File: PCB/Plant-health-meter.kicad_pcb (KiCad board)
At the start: 4 copper layers, 121.2 x 25 mm, 74 parts, among them J1 Conn_01x02, J2 Conn_01x02, J3 Conn_01x04, J4 UJ2-MIBH2-4-SMT-TR, J5 Conn_01x02, Q1 AO3401A, SW1 Boot, SW2 Reset, U1 LTC4412xS6, U2 TPS62172DSG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

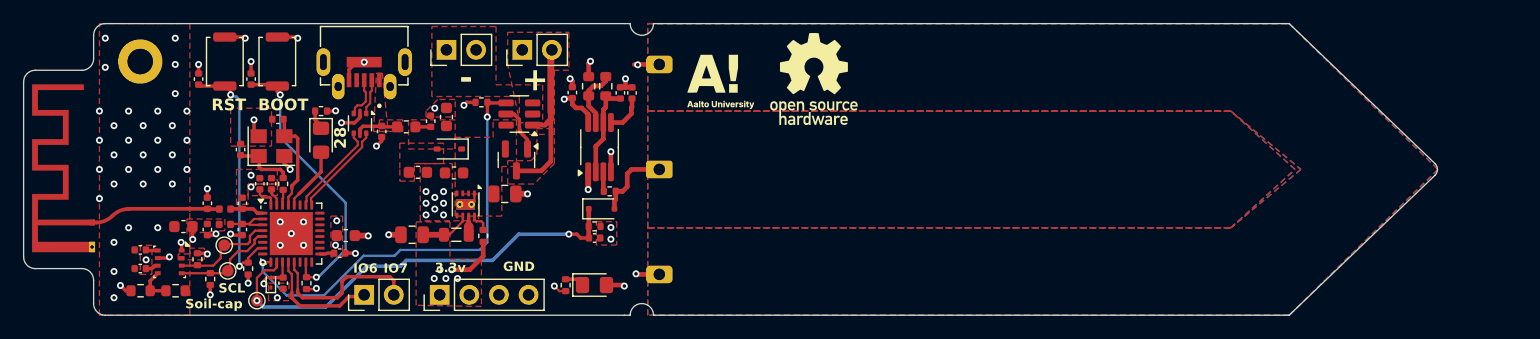
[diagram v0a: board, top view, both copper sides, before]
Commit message: Added battery charging circuit and created WiFi api in firmware + created simple server for esp to send data to
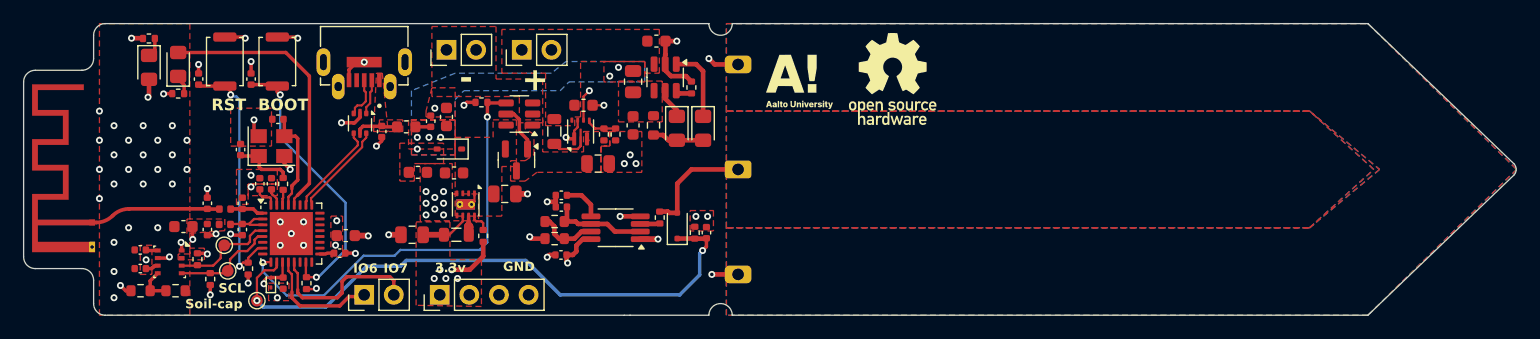
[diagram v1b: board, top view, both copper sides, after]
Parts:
- removed H1: MountingHole, MountingHole:MountingHole_2.2mm_M2_DIN965_Pad
- added C1: 10u, Capacitor_SMD:C_0603_1608Metric, F.Cu at (142.0, 107.0)
- added C27: 10u, Capacitor_SMD:C_0603_1608Metric, F.Cu at (148.2, 101.5)
- added C28: 22u, Capacitor_SMD:C_0805_2012Metric, F.Cu at (143.2, 112.0)
- added C29: 10u, Capacitor_SMD:C_0603_1608Metric, F.Cu at (146.2, 108.7)
- added D1: LED, LED_SMD:LED_0805_2012Metric_Pad1.15x1.40mm_HandSolder, F.Cu at (152.2, 109.0)
- added D6: LED, LED_SMD:LED_0805_2012Metric_Pad1.15x1.40mm_HandSolder, F.Cu at (150.0, 109.0)
- added L5: 1u, Inductor_SMD:L_0805_2012Metric, F.Cu at (139.5, 109.2)
- added R18: 1k, Resistor_SMD:R_0603_1608Metric, F.Cu at (148.0, 108.7)
- added R19: 10k, Resistor_SMD:R_0402_1005Metric, F.Cu at (151.2, 105.5)
- added R2: 570k, Resistor_SMD:R_0402_1005Metric, F.Cu at (143.8, 109.5)
- added R20: 0.3, Resistor_SMD:R_0805_2012Metric, F.Cu at (146.2, 105.0)
- added R3: 100k, Resistor_SMD:R_0402_1005Metric, F.Cu at (144.8, 109.5)
- added U6: TPS61022, Package_DFN_QFN:Texas_RWU0007A_VQFN-7_2x2mm_P0.5mm, F.Cu at (141.8, 109.2)
- added U8: TP4057, Package_TO_SOT_SMD:TSOT-23-6, F.Cu at (149.0, 104.6)
- moved D2 42.5 mm to (104.8, 103.8), turned to -90 degrees
- moved R5 41.5 mm to (104.7, 101.3), turned to 180 degrees
- moved C24 14.0 mm to (140.1, 119.8), turned to 180 degrees
- moved D4 13.9 mm to (107.2, 103.5), turned to 90 degrees
- moved R14 13.4 mm to (139.5, 118.4), turned to 180 degrees
- moved R16 12.4 mm to (139.5, 117.0), turned to 0 degrees
- moved R10 12.3 mm to (107.2, 106.0), turned to 180 degrees
- moved C25 11.0 mm to (140.1, 115.7), turned to 180 degrees
- moved C23 10.7 mm to (140.1, 114.7), turned to 180 degrees
- moved C26 9.60 mm to (152.5, 117.9), turned to -90 degrees
- moved R17 8.60 mm to (151.5, 117.9), turned to -90 degrees
- moved U7 7.04 mm to (144.8, 117.5), turned to 180 degrees
- moved G*** 6.75 mm to (160.5, 105.0)
- moved G*** 6.75 mm to (168.5, 104.8)
- moved S1 6.75 mm to (154.2, 125.0)
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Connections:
- Q1 pad 3: +BATT -> /PWR/source
- U1 pad 1: +BATT -> /PWR/source
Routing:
- net /MCU/DEBUG: track 5.48 -> 23.9 mm
- net +BATT: track 14.6 -> 0.35 mm
- net /MCU/Soil_cap: track 38.4 -> 52.1 mm
- net GND: track 34.1 -> 44.2 mm, vias 75 -> 73
- net Net-(D1-K): track 0.00 -> 6.42 mm
- net Net-(D1-A): track 0.00 -> 4.44 mm
- net Net-(U6-SW): track 0.00 -> 3.31 mm
- net /Sensors/sensor_cap: track 6.71 -> 9.77 mm
- net +3.3V: track 34.0 -> 36.7 mm, vias 21 -> 22
- net Net-(U6-FB): track 0.00 -> 2.69 mm
- net Net-(D6-K): track 0.00 -> 2.61 mm
- net Net-(U8-PROG): track 0.00 -> 1.40 mm
- net +5V: vias 0 -> 6
- added copper zone on B.Cu, net +5V
- added copper zone on F.Cu, net /PWR/charge
- added copper zone on F.Cu, net /PWR/source
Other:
- board size 121.2 x 25 mm -> 128 x 25 mm
- board text removed: "28"

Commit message: Updated some component packages
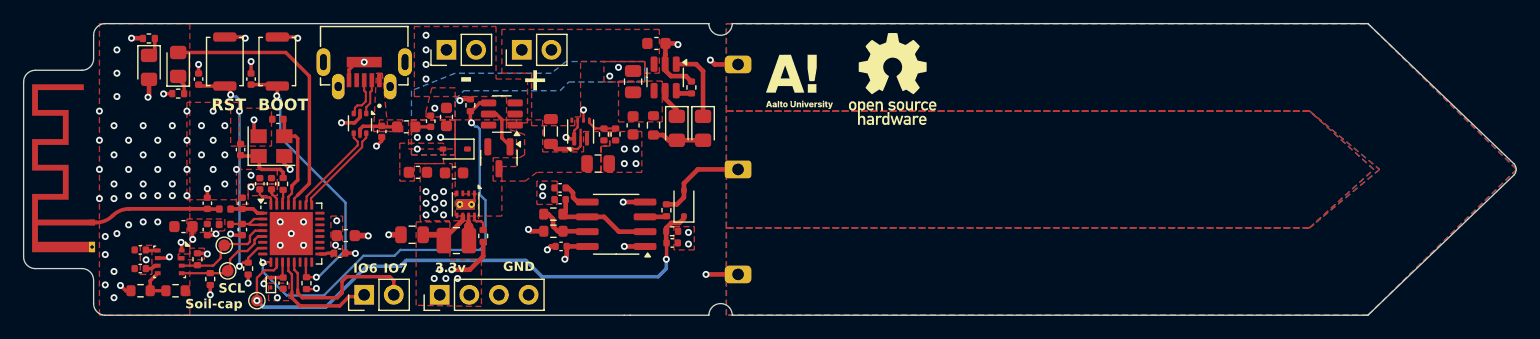
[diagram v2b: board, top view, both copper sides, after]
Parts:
- removed C1: 10u, Capacitor_SMD:C_0603_1608Metric
- removed C1: 22u, Capacitor_SMD:C_0805_2012Metric
- removed U7: TLC555xPS, Package_SO:VSSOP-8_3x3mm_P0.65mm
- added U9: TLC555xD, Package_SO:SOIC-8_3.9x4.9mm_P1.27mm, F.Cu at (144.8, 117.2)
- L2: footprint Inductor_SMD:L_0805_2012Metric -> Inductor_SMD:L_1008_2520Metric
- moved C26 3.07 mm to (149.6, 118.8), turned to 180 degrees
- moved D8 2.01 mm to (150.6, 115.4)
- moved R17 1.94 mm to (149.6, 117.8), turned to 180 degrees
- moved Q1 1.51 mm to (134.8, 111.5)
- moved U1 1.50 mm to (135.0, 107.8)
- moved R1 0.98 mm to (132.3, 107.0), turned to -90 degrees
- moved R15 0.85 mm to (149.1, 116.0)
- moved C24 0.73 mm to (140.1, 119.1)
- moved R14 0.64 mm to (139.4, 117.8)
- moved R16 0.64 mm to (139.4, 116.3)
- moved C23 0.64 mm to (140.0, 114.1)
- moved C25 0.64 mm to (140.0, 115.1)
- moved D5 0.50 mm to (131.0, 110.8)
- moved L2 0.50 mm to (131.1, 118.6)
- moved L5 0.30 mm to (139.2, 109.2)
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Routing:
- net /MCU/Soil_cap: track 52.1 -> 47.9 mm
- net GND: track 44.2 -> 41.1 mm, vias 73 -> 101
- net /Sensors/sensor_cap: track 9.77 -> 8.09 mm
- net Net-(U9-CV): track 3.39 -> 2.59 mm
- net Net-(U9-THR): track 8.21 -> 9.00 mm
- net /Sensors/Q: track 1.34 -> 1.86 mm
